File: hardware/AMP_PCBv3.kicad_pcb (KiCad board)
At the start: 2 copper layers, 70 x 70 mm, 70 parts, among them CN10 Male_R2, CN7 Male_L1, J1 Input_PWR, J2 USB_C_Receptacle_USB2.0_16P, M1 Brake, U1 TPS56624x, U2 RFM95W-915S2, U3 FT230XS, U4 VNH5200A-E, U5 ICM-20948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

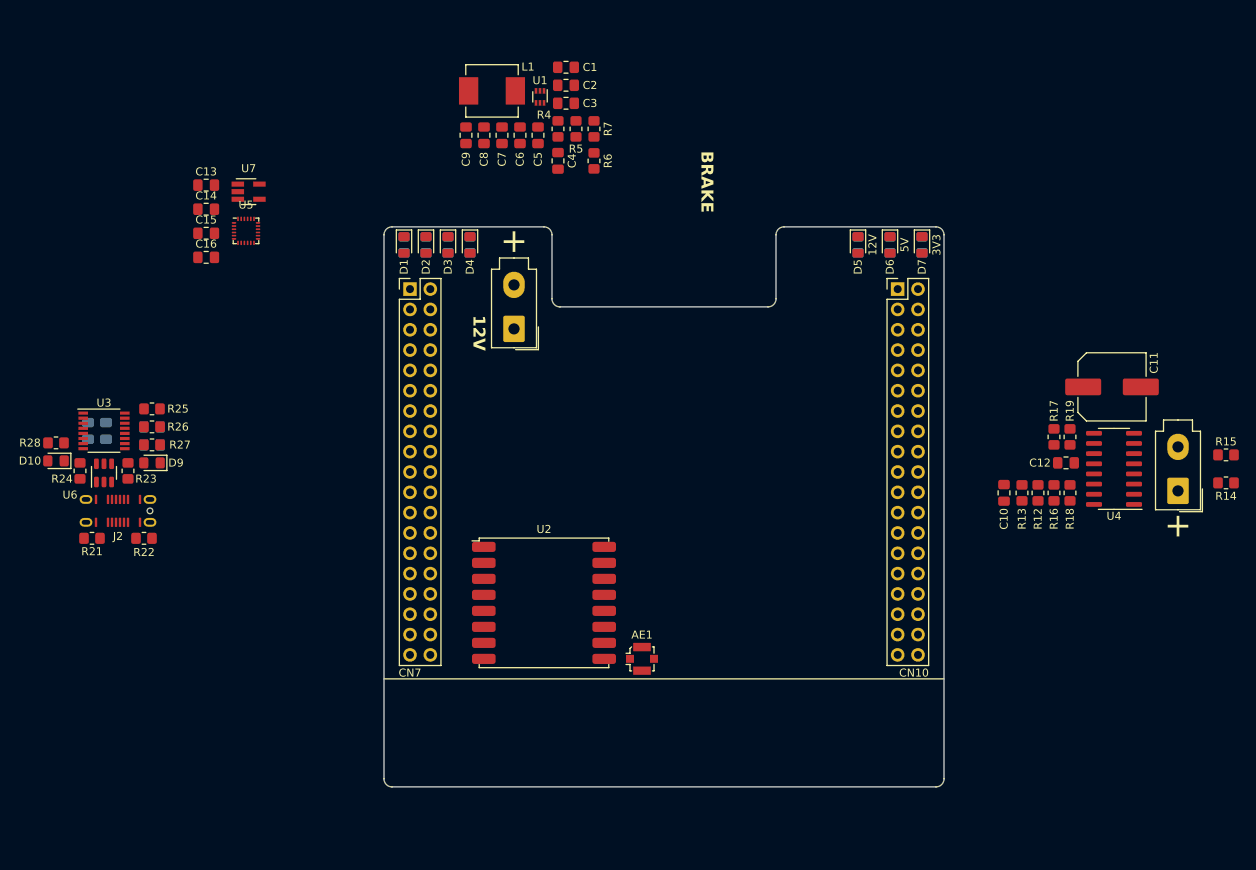
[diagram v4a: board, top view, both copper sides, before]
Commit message: Add fan headers and place components
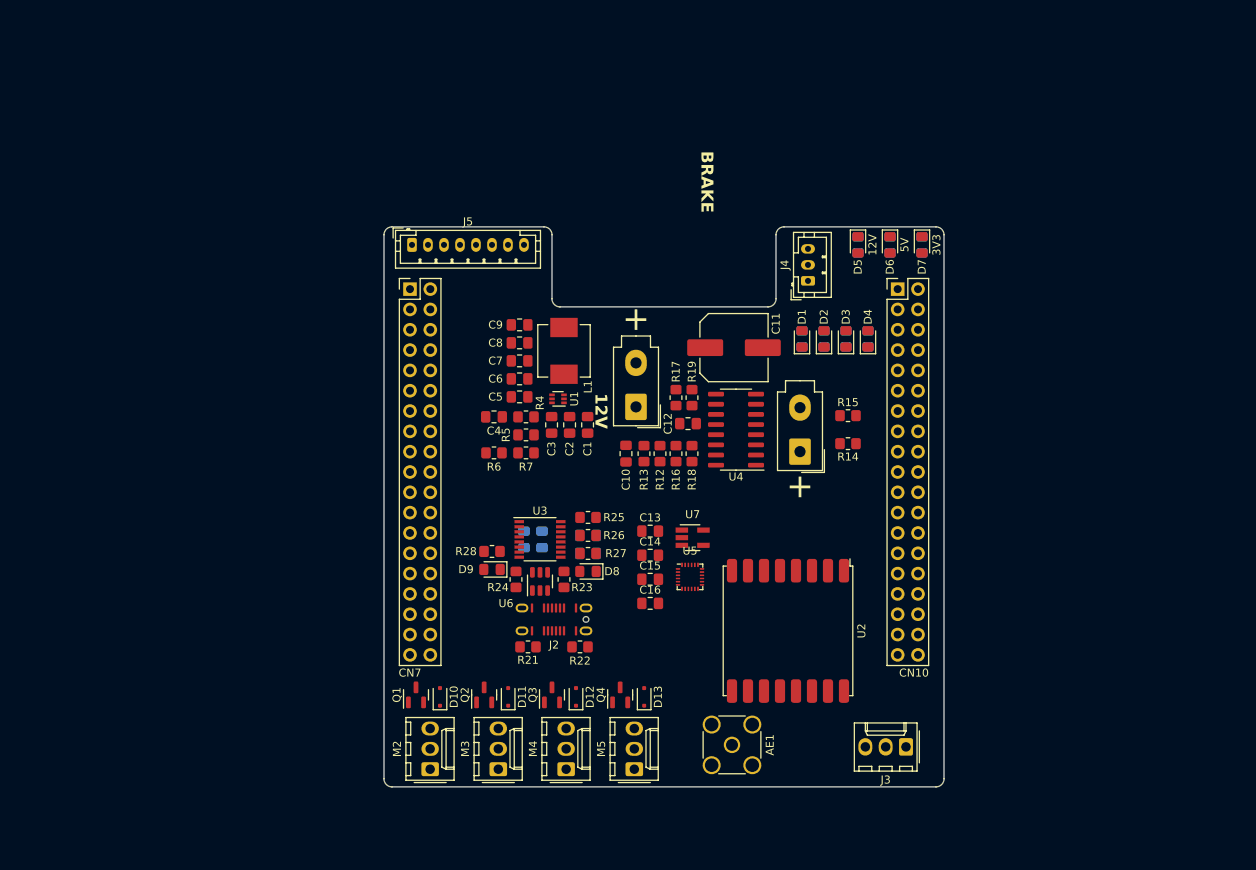
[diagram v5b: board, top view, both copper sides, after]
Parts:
- added D10: D, Diode_SMD:D_SOD-323F, F.Cu at (115.8, 127.2)
- added D11: D, Diode_SMD:D_SOD-323F, F.Cu at (124.3, 127.2)
- added D12: D, Diode_SMD:D_SOD-323F, F.Cu at (132.8, 127.2)
- added D13: D, Diode_SMD:D_SOD-323F, F.Cu at (141.3, 127.2)
- added J3: LED_Header, Connector_Molex:Molex_KK-254_AE-6410-03A_1x03_P2.54mm_Vertical, F.Cu at (174.0, 133.5)
- added J4: VESC_PPM, Connector_JST:JST_PH_B3B-PH-K_1x03_P2.00mm_Vertical, F.Cu at (161.8, 75.2)
- added J5: VESC_COMM, Connector_JST:JST_PH_B8B-PH-K_1x08_P2.00mm_Vertical, F.Cu at (112.2, 70.8)
- added M2: Fan_PC_3pin, Connector_Molex:Molex_KK-254_AE-6410-03A_1x03_P2.54mm_Vertical, F.Cu at (114.5, 136.3)
- added M3: Fan_PC_3pin, Connector_Molex:Molex_KK-254_AE-6410-03A_1x03_P2.54mm_Vertical, F.Cu at (123.0, 136.3)
- added M4: Fan_PC_3pin, Connector_Molex:Molex_KK-254_AE-6410-03A_1x03_P2.54mm_Vertical, F.Cu at (131.5, 136.3)
- added M5: Fan_PC_3pin, Connector_Molex:Molex_KK-254_AE-6410-03A_1x03_P2.54mm_Vertical, F.Cu at (140.0, 136.3)
- added Q1: DMN2310U, Package_TO_SOT_SMD:SOT-23, F.Cu at (112.8, 127.0)
- added Q2: DMN2310U, Package_TO_SOT_SMD:SOT-23, F.Cu at (121.3, 127.0)
- added Q3: DMN2310U, Package_TO_SOT_SMD:SOT-23, F.Cu at (129.8, 127.0)
- added Q4: DMN2310U, Package_TO_SOT_SMD:SOT-23, F.Cu at (138.3, 127.0)
- AE1: footprint Connector_Coaxial:U.FL_Molex_MCRF_73412-0110_Vertical -> Connector_Coaxial:SMA_Amphenol_132291_Vertical
- moved C13 70.4 mm to (142.0, 106.5)
- moved C14 70.4 mm to (142.0, 109.5)
- moved C15 70.4 mm to (142.0, 112.5)
- moved C16 70.4 mm to (142.0, 115.6)
- moved U5 70.4 mm to (147.0, 112.2)
- moved U7 70.4 mm to (147.3, 107.3)
- moved C21 56.2 mm to (128.5, 107.6)
- moved C22 56.2 mm to (134.2, 109.3)
- moved C23 56.2 mm to (126.2, 107.6)
- moved C24 56.2 mm to (134.2, 107.1)
- moved D8 56.2 mm to (134.2, 111.6)
- moved D9 56.2 mm to (122.2, 111.3)
- moved J2 56.2 mm to (130.0, 119.0)
- moved R21 56.2 mm to (126.8, 121.0)
- moved R22 56.2 mm to (133.2, 121.0)
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- renumbered D9 to D8, D10 to D9
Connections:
- C10 pad 1: /Brake Controller/CS -> /BRAKE_CS
- CN10 pad 13: /PA6 -> /BRAKE_INB
- CN10 pad 15: /PA7 -> /BRAKE_INA
- CN10 pad 16: /PB12 -> /BRAKE_ENA
- CN10 pad 19: /PC7 -> /BRAKE_CS
- CN10 pad 24: /PB1 -> /LED_SIG
- CN10 pad 33: /PA10 -> /IMU_CS
- CN10 pad 34: /PC4 -> /IMU_INT1
- CN10 pad 6: /PC5 -> /BRAKE_ENB
- D1 pad 2: unconnected-(D1-A-Pad2) -> /PC8
- D2 pad 2: unconnected-(D2-A-Pad2) -> /PB8
- D3 pad 2: unconnected-(D3-A-Pad2) -> /PC6
- D4 pad 2: unconnected-(D4-A-Pad2) -> /PB9
- R13 pad 1: /Brake Controller/CS -> /BRAKE_CS
- R14 pad 1: /Brake Controller/IN_A -> /BRAKE_INA
- R15 pad 2: /Brake Controller/IN_B -> /BRAKE_INB
- R16 pad 1: /Brake Controller/EN_A -> /BRAKE_ENA
- R17 pad 2: /Brake Controller/EN_B -> /BRAKE_ENB
- U2 pad 14: unconnected-(U2-DIO0-Pad14) -> /PB5
- U2 pad 2: unconnected-(U2-MISO-Pad2) -> /PB14
- U2 pad 3: unconnected-(U2-MOSI-Pad3) -> /PB15
- U2 pad 4: unconnected-(U2-SCK-Pad4) -> /PB10
- U2 pad 5: unconnected-(U2-NSS-Pad5) -> /PB13
- U2 pad 6: unconnected-(U2-RESET-Pad6) -> /PB4
- U3 pad 1: /Jetson USB/TX -> /PA1
- U3 pad 4: /Jetson USB/RX -> /PA0
- U5 pad 12: /IMU/INT1 -> /IMU_INT1
- U5 pad 22: /IMU/CS -> /IMU_CS
- U5 pad 23: /IMU/CLK -> /PB10
- U5 pad 24: /IMU/MISO -> /PB14
- U5 pad 9: /IMU/MOSI -> /PB15

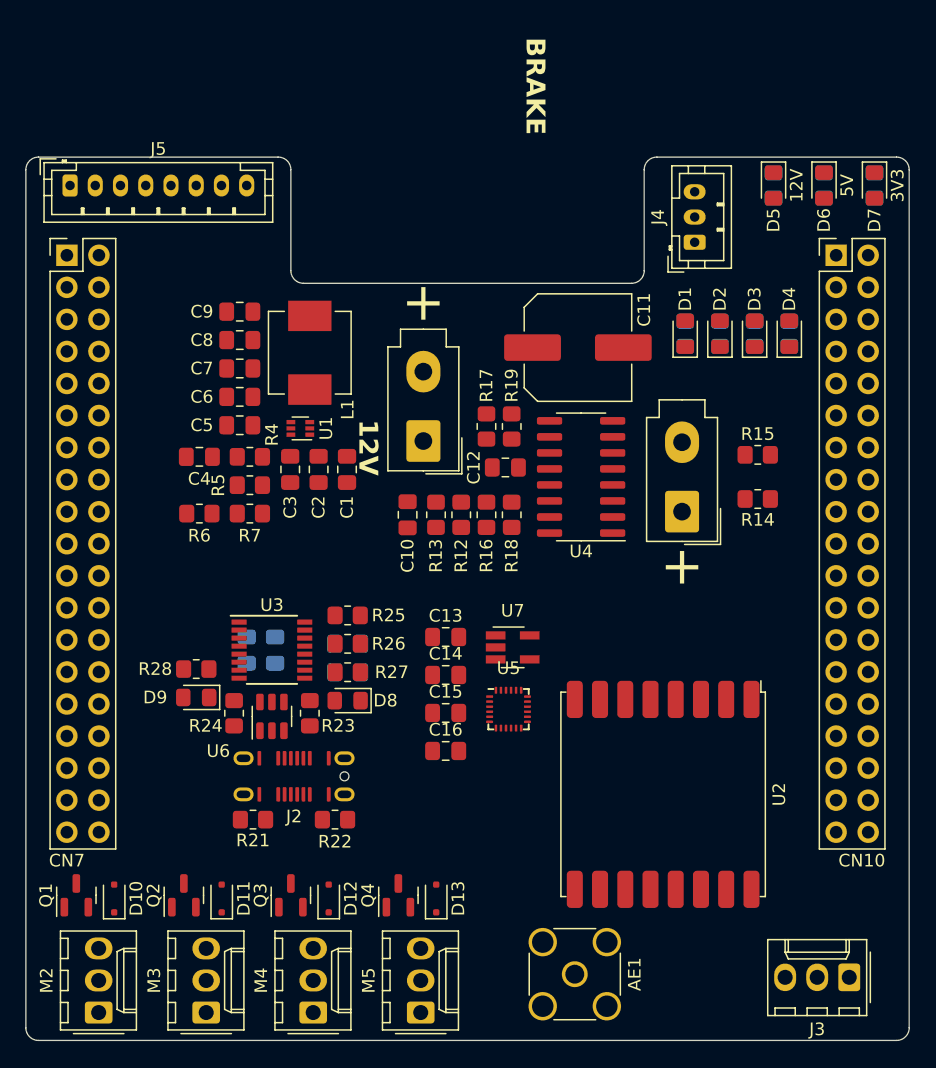
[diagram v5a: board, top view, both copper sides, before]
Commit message: Add steering connector and route board (4 layers)
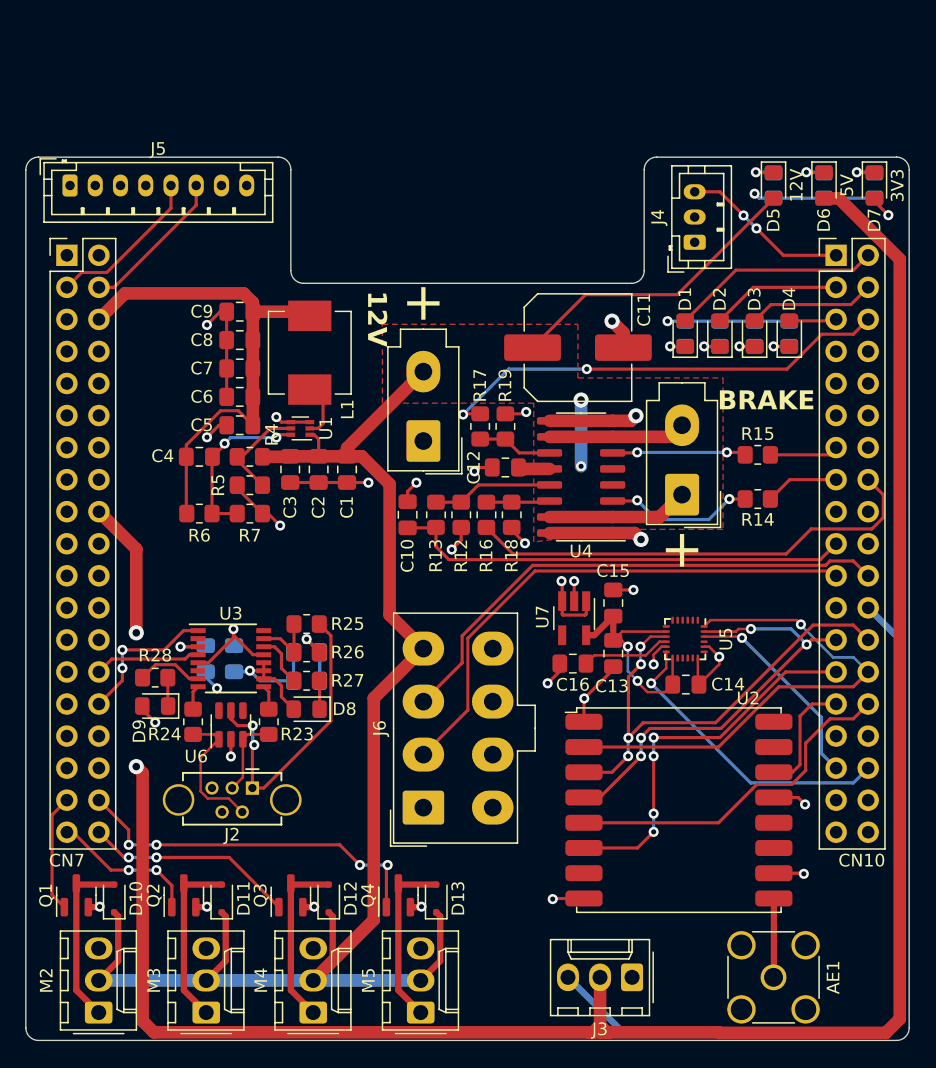
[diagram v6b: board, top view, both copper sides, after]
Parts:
- removed R21, R22: 5.1k, Resistor_SMD:R_0805_2012Metric_Pad1.20x1.40mm_HandSolder
- added J6: STEERING, Connector_Molex:Molex_Mini-Fit_Jr_5566-08A_2x04_P4.20mm_Vertical, F.Cu at (140.2, 120.0)
- J2: value USB_C_Receptacle_USB2.0_16P -> USB_B_Mini; footprint AMP_Custom:USB_C_Receptacle_GCT_USB4145 -> AMP_Custom:USB_Mini-B_Adam_Tech_MUSB-B5-S-VT-02_Vertical_CircularHoles
- moved C14 19.0 mm to (161.1, 110.3)
- moved J3 17.2 mm to (156.8, 133.5)
- moved C15 15.9 mm to (155.3, 103.8), turned to 90 degrees
- moved AE1 15.8 mm to (168.0, 133.5)
- moved U5 15.1 mm to (161.0, 106.7), turned to -90 degrees
- moved C13 13.3 mm to (155.3, 107.8), turned to -90 degrees
- moved C16 12.2 mm to (152.1, 108.6), turned to 180 degrees
- moved U7 5.39 mm to (152.2, 105.0), turned to -90 degrees
- moved J2 4.93 mm to (125.1, 118.5)
- moved C21 3.32 mm to (125.2, 108.2)
- moved C22 3.32 mm to (131.0, 110.0)
- moved C23 3.32 mm to (123.0, 108.2)
- moved C24 3.32 mm to (131.0, 107.8)
- moved D8 3.32 mm to (131.0, 112.2)
- moved D9 3.32 mm to (119.0, 112.0)
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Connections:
- J4 pad 1: /VESC_GND -> GND
- J5 pad 3: /VESC_GND -> GND
- J5 pad 5: /VESC_RX -> /PC12
- J5 pad 6: /VESC_TX -> /PD2
- U6 pad 4: /Jetson USB/D- -> unconnected-(U6-I/O2-Pad4)
- U6 pad 6: /Jetson USB/D+ -> unconnected-(U6-I/O1-Pad6)
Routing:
- net +5V: track 0.00 -> 177.3 mm, vias 0 -> 2
- net +12V: track 0.00 -> 148.4 mm, vias 0 -> 2
- net GND: track 0.00 -> 111.3 mm, vias 0 -> 29
- net /LED_SIG: track 0.00 -> 62.2 mm
- net /PA9: track 0.00 -> 42.2 mm
- net /PB2: track 0.00 -> 41.6 mm
- net /E5V: track 0.00 -> 40.0 mm
- net /PB14: track 0.00 -> 39.9 mm, vias 0 -> 1
- net /PB15: track 0.00 -> 38.7 mm, vias 0 -> 4
- net /BRAKE_ENA: track 0.00 -> 37.0 mm
- net /BRAKE_ENB: track 0.00 -> 36.6 mm, vias 0 -> 2
- net /BRAKE_CS: track 0.00 -> 36.5 mm
- net /PB10: track 0.00 -> 34.8 mm, vias 0 -> 4
- net +3V3: track 0.00 -> 32.3 mm, vias 0 -> 8
- net /PB4: track 0.00 -> 30.1 mm, vias 0 -> 4
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- added copper zone on F.Cu, net +12V
- added copper zone on In1.Cu, net +3V3
- added copper zone on In2.Cu, net GND
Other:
- copper layers 2 -> 4

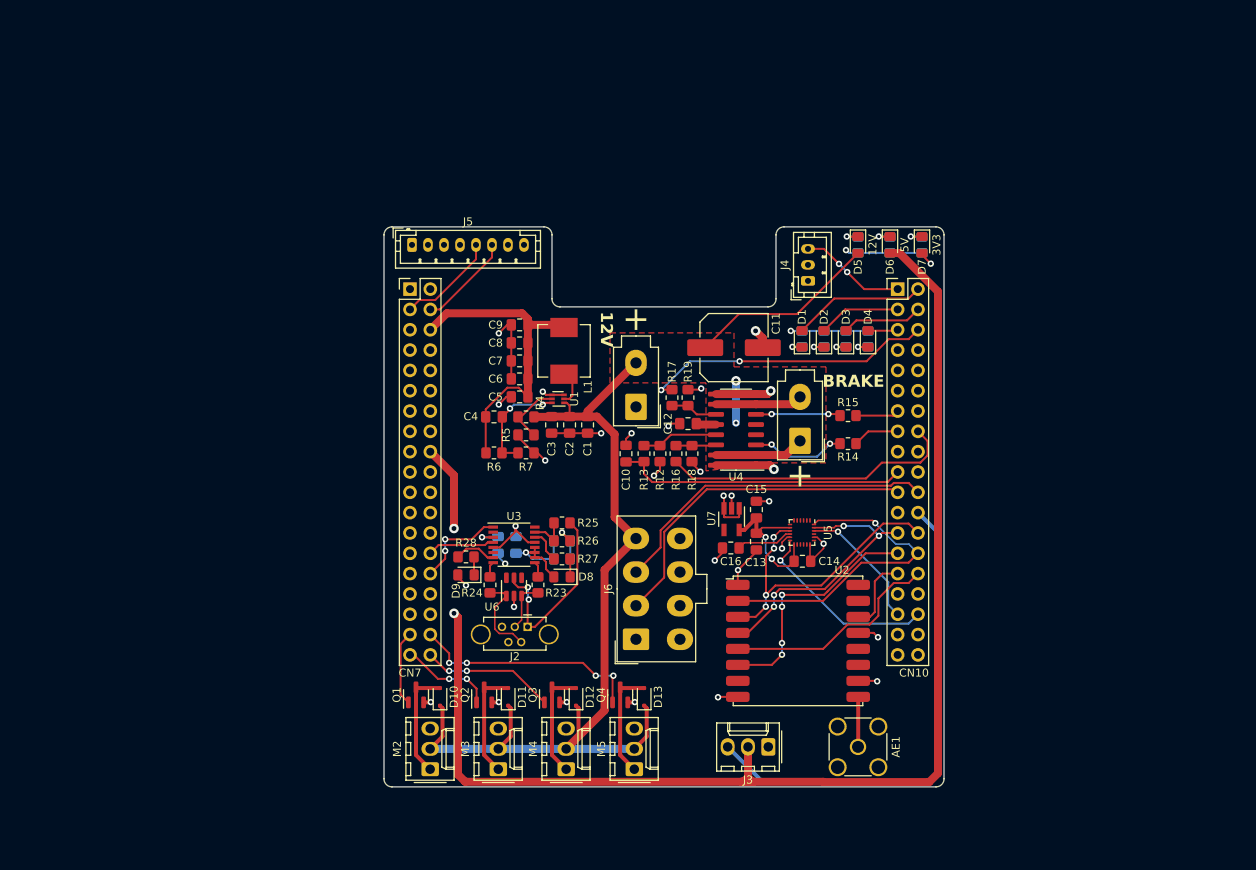
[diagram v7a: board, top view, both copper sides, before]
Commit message: Resize board and begin new layout
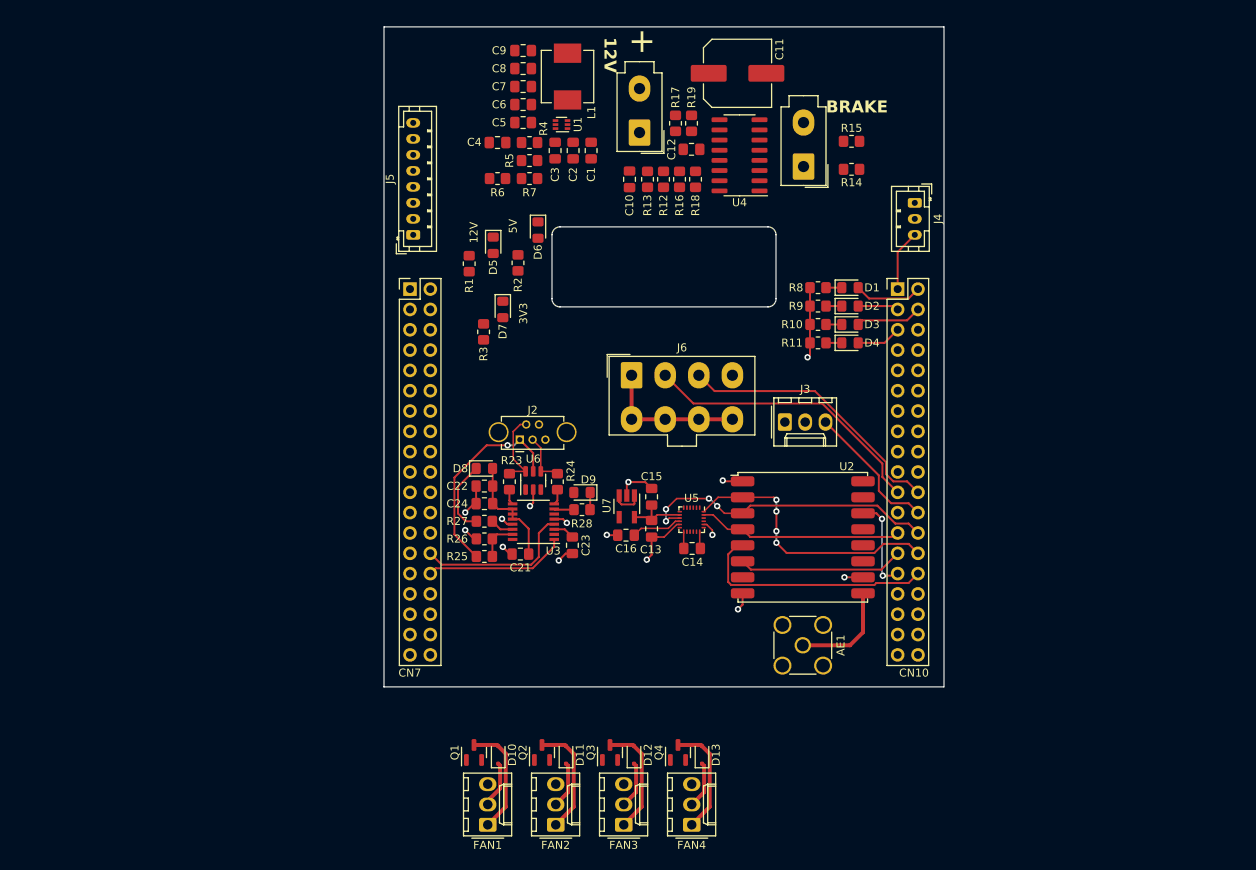
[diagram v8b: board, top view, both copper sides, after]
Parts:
- C21, C22, C23, C24, R1, R10, R11, R2, R3, R8, R9: moved to F.Cu
- moved R3 55.9 mm to (121.2, 81.6)
- moved D7 53.0 mm to (123.6, 78.8)
- moved R1 48.7 mm to (119.4, 73.1)
- moved R2 46.6 mm to (125.5, 73.0)
- moved D5 45.6 mm to (122.4, 70.8)
- moved D6 44.0 mm to (128.0, 68.9)
- moved J3 40.7 mm to (158.9, 92.9), turned to 0 degrees
- moved C1 34.3 mm to (134.6, 59.0)
- moved C10 34.3 mm to (139.4, 62.6)
- moved C11 34.3 mm to (152.9, 49.3)
- moved C12 34.3 mm to (147.2, 58.8)
- moved C2 34.3 mm to (132.4, 59.0)
- moved C3 34.3 mm to (130.1, 59.0)
- moved C4 34.3 mm to (122.9, 58.0)
- moved C5 34.3 mm to (126.1, 55.5)
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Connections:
- J2 pad 2: /Jetson USB/D+ -> /Jetson USB/D-
- J2 pad 3: /Jetson USB/D- -> /Jetson USB/D+
- Q2 pad 1: /PC3 -> /PC1
- Q4 pad 1: /PC1 -> /PC3
- U6 pad 1: /Jetson USB/D+ -> unconnected-(U6-I/O1-Pad1)
- U6 pad 3: /Jetson USB/D- -> unconnected-(U6-I/O2-Pad3)
- U6 pad 4: unconnected-(U6-I/O2-Pad4) -> /Jetson USB/D+
- U6 pad 6: unconnected-(U6-I/O1-Pad6) -> /Jetson USB/D-
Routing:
- net +5V: track 177.3 -> 0.00 mm, vias 2 -> 0
- net +12V: track 148.4 -> 23.4 mm, vias 2 -> 0
- net /LED_SIG: track 62.2 -> 17.4 mm
- net GND: track 111.3 -> 66.8 mm, vias 29 -> 15
- net /E5V: track 40.0 -> 0.00 mm
- net /BRAKE_ENA: track 37.0 -> 0.00 mm
- net /BRAKE_ENB: track 36.6 -> 0.00 mm, vias 2 -> 0
- net /BRAKE_CS: track 36.5 -> 0.00 mm
- net /PC1: track 29.1 -> 0.00 mm, vias 4 -> 0
- net /IMU_INT1: track 24.0 -> 0.00 mm, vias 1 -> 0
- net /PC0: track 16.7 -> 0.00 mm, vias 2 -> 0
- net /IMU_CS: track 16.5 -> 0.00 mm, vias 1 -> 0
- net Net-(U1-FB): track 13.5 -> 0.00 mm, vias 2 -> 0
- net /PC12: track 12.6 -> 0.00 mm
- net /PD2: track 12.0 -> 0.00 mm
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- removed copper zone on F.Cu, net +12V
- removed copper zone on In1.Cu, net +3V3
- removed copper zone on In2.Cu, net GND
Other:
- board size 70 x 70 mm -> 70 x 82.5 mm
- copper layers 4 -> 2
- board text added: "FAN1"
- board text added: "FAN2"
- board text added: "FAN3"
- board text added: "FAN4"
